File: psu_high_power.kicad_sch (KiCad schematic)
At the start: 5 parts, among them U5 CH224K

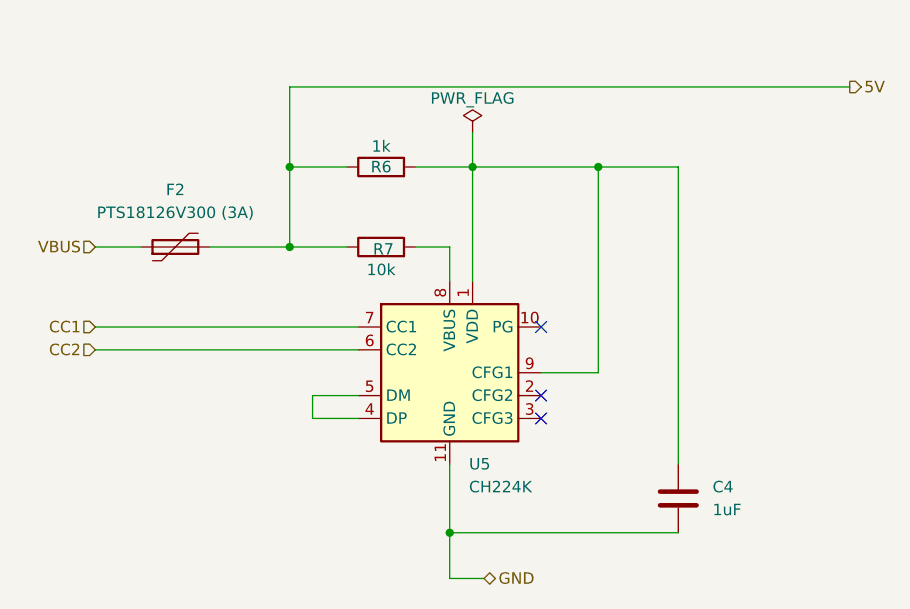
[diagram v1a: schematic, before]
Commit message: Tied down CFG2,3 to GND.
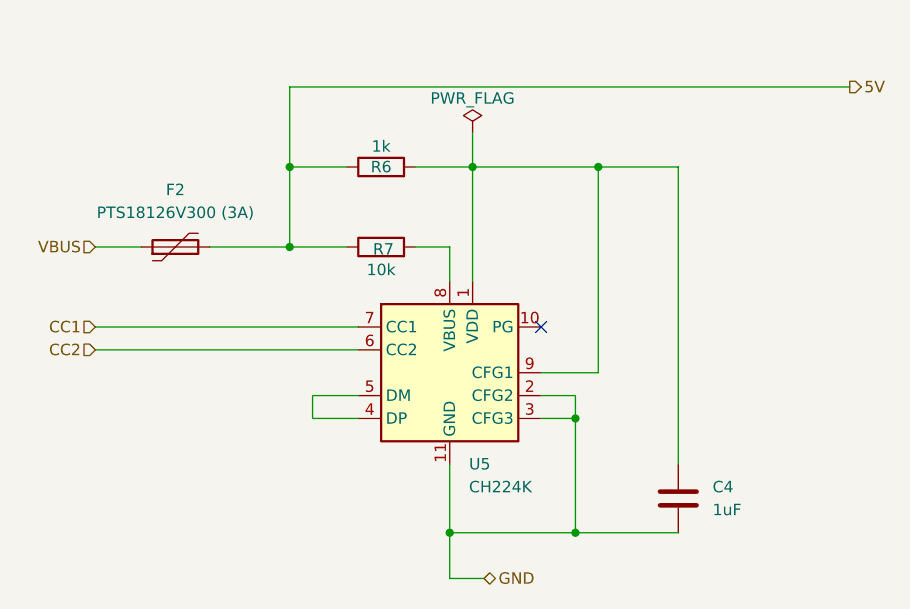
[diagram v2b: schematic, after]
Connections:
- net GND: now also U5.2 (CFG2), U5.3 (CFG3)
- no-connect marks 3 -> 1
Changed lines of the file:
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@@
+	)
+	(junction
+		(at 96.52 62.23)
+		(diameter 0)
+		(color 0 0 0 0)
+	)
+	(junction
+		(at 96.52 74.93)
+		(diameter 0)
+		(color 0 0 0 0)
 	)
 	(junction
@@
 	)
 	(no_connect
-		(at 92.71 62.23)
-	)
-	(no_connect
-		(at 92.71 59.69)
-	)
-	(no_connect
 		(at 92.71 52.07)
 	)
@@
 	(wire
 		(pts
-			(xy 82.55 74.93) (xy 107.95 74.93)
+			(xy 96.52 59.69) (xy 96.52 62.23)
+		)
+		(stroke
+			(width 0)
+			(type default)
+		)
+	)
+	(wire
+		(pts
+			(xy 82.55 74.93) (xy 96.52 74.93)
 		)
 		(stroke
@@
 	(wire
 		(pts
+			(xy 92.71 62.23) (xy 96.52 62.23)
+		)
+		(stroke
+			(width 0)
+			(type default)
+		)
+	)
+	(wire
+		(pts
 			(xy 85.09 30.48) (xy 85.09 34.29)
 		)
@@
 	(wire
 		(pts
+			(xy 92.71 59.69) (xy 96.52 59.69)
+		)
+		(stroke
+			(width 0)
+			(type default)
+		)
+	)
+	(wire
+		(pts
 			(xy 85.09 34.29) (xy 99.06 34.29)
 		)
@@
 	(wire
 		(pts
+			(xy 96.52 62.23) (xy 96.52 74.93)
+		)
+		(stroke
+			(width 0)
+			(type default)
+		)
+	)
+	(wire
+		(pts
 			(xy 67.31 62.23) (xy 72.39 62.23)
 		)
 		(stroke
+			(width 0)
+			(type default)
+		)
+	)
+	(wire
+		(pts
+			(xy 96.52 74.93) (xy 107.95 74.93)
+		)
+		(stroke

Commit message: Added decoupling caps for the AMS1117-3.3
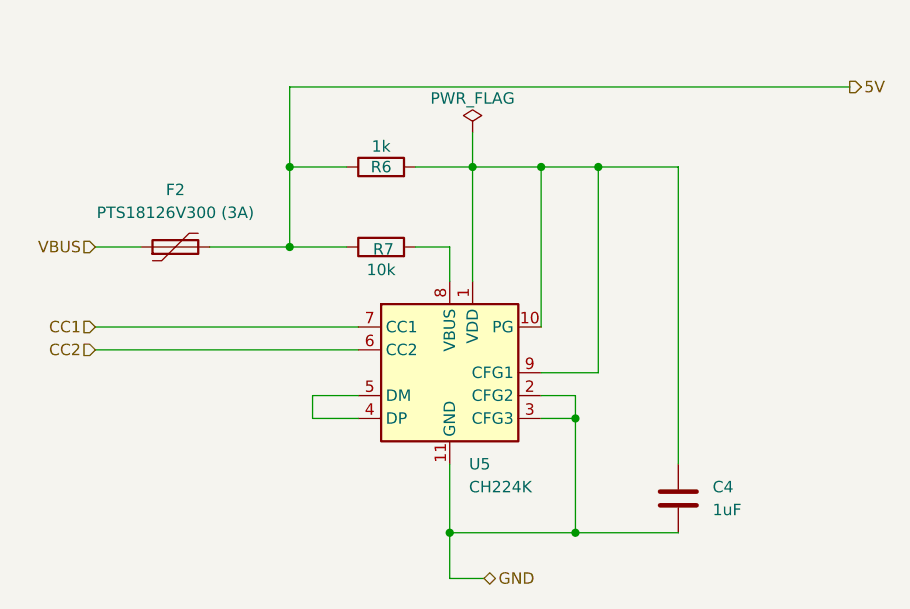
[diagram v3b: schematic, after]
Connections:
- net at C4.1, R6.2, U5.1 (VDD)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: now also U5.10 (PG)
- no-connect marks 1 -> 0
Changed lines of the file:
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@@
+	)
+	(junction
+		(at 92.71 34.29)
+		(diameter 0)
+		(color 0 0 0 0)
 	)
 	(junction
@@
 		(color 0 0 0 0)
 	)
-	(no_connect
-		(at 92.71 52.07)
-	)
 	(wire
 		(pts
@@
 	(wire
 		(pts
+			(xy 92.71 34.29) (xy 99.06 34.29)
+		)
+		(stroke
+			(width 0)
+			(type default)
+		)
+	)
+	(wire
+		(pts
 			(xy 85.09 34.29) (xy 85.09 46.99)
 		)
@@
 	(wire
 		(pts
+			(xy 92.71 34.29) (xy 92.71 52.07)
+		)
+		(stroke
+			(width 0)
+			(type default)
+		)
+	)
+	(wire
+		(pts
 			(xy 82.55 74.93) (xy 96.52 74.93)
 		)
@@
 	(wire
 		(pts
-			(xy 85.09 34.29) (xy 99.06 34.29)
-		)
-		(stroke
+			(xy 85.09 34.29) (xy 92.71 34.29)
+		)
+		(stroke

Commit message: Moved some components around for better readability.
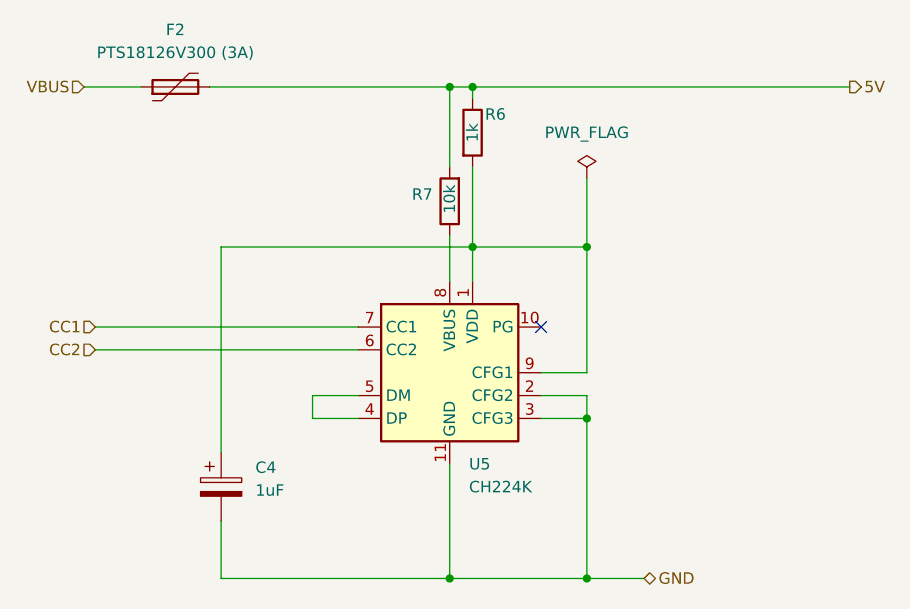
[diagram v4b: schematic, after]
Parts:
- removed C4: 1uF, symbol Device:C
- added C4: 1uF, symbol Device:C_Polarized
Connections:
- net 5V: now also R7.2; no longer R7.1
- net GND: now also C4.2
- net at R6.2, U5.1 (VDD), U5.9 (CFG1): now also C4.1; no longer U5.10 (PG)
- net at U5.8 (VBUS): now also R7.1; no longer R7.2
- no-connect marks 0 -> 1
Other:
- moved on the sheet: F2, R6, R7

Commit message: Updated README.
Reworked the circuit around CH224K per datasheet an example schematics.
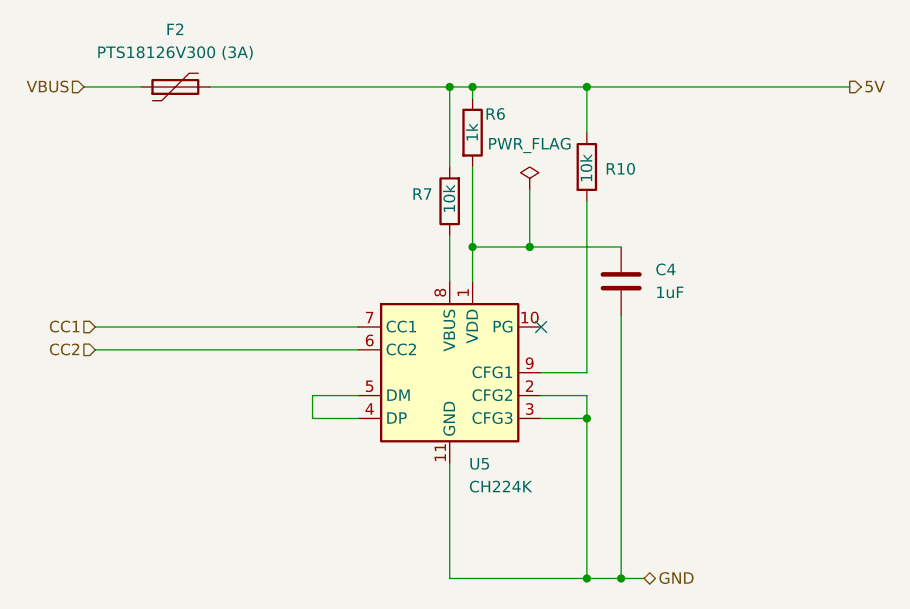
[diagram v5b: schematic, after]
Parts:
- removed C4: 1uF, symbol Device:C_Polarized
- added C4: 1uF, symbol Device:C
- added R10: 10k, symbol Device:R
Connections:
- net 5V: now also R10.1
- net GND: now also C4.2
- net at R6.2, U5.1 (VDD): now also C4.1; no longer U5.9 (CFG1)
- new net: R10.2, U5.9 (CFG1)

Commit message: Reorganized board to be on one sheet.
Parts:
- removed C4: 1uF, symbol Device:C
- removed F2: PTS18126V300 (3A), symbol Device:Polyfuse
- removed R10, R7: 10k, symbol Device:R
- removed R6: 1k, symbol Device:R
- removed U5: CH224K, Package_SO:SSOP-10-1EP_3.9x4.9mm_P1mm_EP2.1x3.3mm, symbol Interface_USB:CH224K
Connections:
- no-connect marks 1 -> 0
